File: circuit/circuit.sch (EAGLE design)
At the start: 56 parts, among them IC1 74HC86N, IC2 74HC86N, IC3 74HC30N, IC4 74HC86N

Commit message: updated circuit (layout needs to be done next)
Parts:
- removed CM4, CM5, CM6: 100nF, rcl:C-EU025-025X050
- removed H1, H2, H3, H4: MOUNT-HOLE3.2, holes:MOUNT-HOLE3.2
- removed IC2, IC4: 74HC86N, 74xx-eu:74HC86N
- removed IC3: 74HC30N, 74xx-eu:74HC30N
- removed JP1: IN, pinhead:PINHD-1X8
- removed JT: (no value), pinhead:PINHD-1X4
- removed RP: 300, rcl:R-EU_0207/10
- removed SJ1, SJ2, SJ3, SJ4, SJ5, SJ6, SJ7, SJ8: (no value), jumper:SJ
- added CS4: 100nF, rcl:C-EU025-025X050
- added LD1, LD2: green, robo_ag:LED-3MM
- added LD3, LD4: yellow, robo_ag:LED-3MM
- added RLD1, RLD2, RLD3, RLD4: 2k, rcl:R-EU_0207/10
- added RN1, RN2, RN3, RN4: 120, resistor-sil:E4R
- added RP1, RP2: 300, rcl:R-EU_0207/10
- added X1: PSS 254/8G, con-molex:22-23-2081
- IC1: value 74HC86N -> 74HC04N; device 74xx-eu:74HC86N -> 74xx-eu:74AC04N
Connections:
- removed net BUS_ERROR: IC3A.O
- removed net DISP_COL_SCK: JP1.6
- removed net DISP_COL_SER: JP1.4
- removed net PROG_MOSI: ICM.PB3(MOSI/OC2), RP.2
- removed net PROG_SCK: ICM.PB5(SCK), JP.3_SCK
- removed net RETURN_LED_LAOD: IC2B.I1
- removed net TWI_SCL: ICM.PC5(ADC5/SCL), JT.1, JT.4
- removed net TWI_SDA: ICM.PC4(ADC4/SDA), JT.2, JT.3
- new net !BUS_RGB: IC1A.I, IC1B.I, ICM.PD1(TXD)
- new net !RETURN_RGB: IC1D.O, ICM.PD0(RXD)
- new net N$32: IC1E.O, RLD2.2
- new net N$33: JP.3_SCK, RP1.2
- new net N$34: LD2.C, RLD2.1
- new net N$35: ICM.PC4(ADC4/SDA)
- new net N$36: ICM.PC5(ADC5/SCL)
- new net N$37: IC1C.O, RLD3.2
- new net N$38: LD3.C, RLD3.1
- new net N$41: IC1F.O, RLD4.1
- new net N$42: LD4.A, RLD4.2
- new net PROG_MOSI_AND_DISP_COL_SER: ICM.PB3(MOSI/OC2), RN3B.1, RP2.2
- new net PROG_SCK_AND_DISP_COL_SCK: ICM.PB5(SCK), RN3D.1, RP1.1
- net +5V: now also CS4.1, LD2.A, LD3.A, X1-2.S; no longer CM4.2, CM5.2, CM6.2, IC2P.VCC, IC4P.VCC, JP1.2, SJ8.1
- net BTN2: now also ICM.PB1(OC1A); no longer ICM.PC3(ADC3)
- net BTN3: now also ICM.PB2(SS/OC1B); no longer ICM.PD4(XCK/T0)
- net BUS_BTN_DATA: now also ICM.PD2(INT0), RN1B.1; no longer IC2A.I0, SV1.8
- net BUS_BTN_LOAD: now also ICM.PD3(INT1), RN2C.2; no longer IC1D.I0, SV1.7
- net BUS_CLK: now also ICM.PD6(AIN0), RN2A.1; no longer IC1A.I0, SV1.2
- net BUS_IR_CLK: now also ICM.PD5(T1), RN1C.1; no longer IC1C.I0, SV1.6
- net BUS_LED_DATA: now also IC1C.I, ICM.PD4(XCK/T0), RN1A.1; no longer IC2C.I0, SV1.10
- net BUS_LED_LOAD: now also ICM.PD7(AIN1), RN2B.2; no longer IC2B.I0, SV1.9
- net BUS_RGB: now also IC1A.O, RN1D.1; no longer IC1B.I0, SV1.4
- net DISP_!ENABLE!: now also ICM.PC3(ADC3), RN4B.1; no longer JP1.8
- net DISP_RCK: now also ICM.PC2(ADC2), RN4A.1; no longer JP1.7
- net DISP_ROW_SCK: now also ICM.PC1(ADC1), RN3C.1; no longer JP1.5
- net DISP_ROW_SER: now also ICM.PC0(ADC0), RN3A.1; no longer JP1.3
- net GND: now also CS4.2, LD1.C, LD4.C, SV1.10, SV1.6, SV1.8, SV2.10, SV2.6, SV2.8, X1-1.S; no longer CM4.1, CM5.1, CM6.1, IC2D.I0, IC2D.I1, IC2P.GND, IC4P.GND, JP1.1, SV1.1, SV1.3, SV1.5, SV2.1, SV2.3, SV2.5
- net N$1: now also RN1A.2, SV1.1; no longer IC3A.I0, SJ1.2
- net N$16: now also RN1D.2, SV1.7; no longer IC3A.I3, SJ4.2
- net N$17: now also RN2A.2, SV1.9; no longer IC3A.I4, SJ5.2
- net N$18: now also RN2C.1, SV1.4; no longer IC3A.I5, SJ6.2
- net N$19: now also RN2B.1, SV1.2; no longer IC3A.I6, SJ7.2
- net N$2: now also RN1B.2, SV1.3; no longer IC3A.I1, SJ2.2
- net N$20: now also RN3A.2, X1-3.S; no longer IC3A.I7, SJ8.2
- net N$21: now also RN3B.2, X1-4.S; no longer IC1A.O, SJ1.1
- net N$22: now also RN3C.2, X1-5.S; no longer IC1B.O, SJ2.1
- net N$23: now also RN3D.2, X1-6.S; no longer IC1C.O, SJ3.1
- net N$24: now also RN4A.2, X1-7.S; no longer IC1D.O, SJ4.1
- net N$25: now also RN4B.2, X1-8.S; no longer IC2A.O, SJ5.1
- net N$26: now also LD1.A, RLD1.2; no longer IC2B.O, SJ6.1
- net N$3: now also RN1C.2, SV1.5; no longer IC3A.I2, SJ3.2
- net N$31: now also IC1B.O, RLD1.1; no longer IC2C.O, SJ7.1
- net PROG_MOSI_1: now also RP2.1; no longer RP.1
- net RETURN_BTN_DATA: now also IC1F.I, SV2.3; no longer IC2A.I1, SV2.8
- net RETURN_BTN_LOAD: now also SV2.4; no longer IC1D.I1, SV2.7
- net RETURN_CLK: now also SV2.9; no longer IC1A.I1, SV2.2
- net RETURN_IR_CLK: now also SV2.5; no longer IC1C.I1, SV2.6
- net RETURN_LED_DATA: now also SV2.1; no longer IC2C.I1, SV2.10
- net RETURN_LED_LOAD: now also SV2.2; no longer SV2.9
- net RETURN_RGB: now also IC1D.I, IC1E.I, SV2.7; no longer IC1B.I1, SV2.4
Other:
- note added: "(also OC0A)"
- note added: "1. Inversion of UART: bus-protocoll for RGB-LED (WS2812B) is invers to UART-Protocoll e.g. idle is low instead of high"
- note added: "2. Additional features: power supply button 3 data leds (RGB, IR, Button)"
- note added: "3. only for self-test: BUS_BTN_DATA RETURN_RGB RETURN_LED_DATA"
- note added: "Additionals"
- note added: "In/Out Lights"
- note added: "Logic"
- note added: "OC0B"
- note added: "Out Display"
- note added: "indicator for receiving a pushed button"
- note added: "indicator for receiving data from last RGB-led"
- note added: "indicator for sending data to RGB-leds"
- note added: "indicator for turning IR-leds on"
- note removed: "Anzeige Connector"
- note removed: "BUS-Driver"
- note removed: "Nochmal drüber nachdenken! Über die Jumper können die gewünschten Signale gewählt werden. Allerdings müssen freie Eingänge mit VDD verbunden werden. Hier ist noch eine clevere Lösung nötig."
- note removed: "Reserve"
- moved on the sheet: CM1, CM2, CM3, CQ1, CQ2, IC1P, ICM, JP, Q1, SV1, SV2

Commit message: Updated Layout
Layout work in progress
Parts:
- removed RN1, RN2, RN3, RN4: 120, resistor-sil:E4R
- added R1, R10, R11, R12, R13, R2, R3, R4, R5, R6, R7, R8, R9: 120, rcl:R-EU_R0805
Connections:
- removed net N$35: ICM.PC4(ADC4/SDA)
- removed net N$36: ICM.PC5(ADC5/SCL)
- net BTN1: now also ICM.PC4(ADC4/SDA); no longer ICM.PB0(ICP)
- net BTN2: now also ICM.PC5(ADC5/SCL); no longer ICM.PB1(OC1A)
- net BUS_BTN_DATA: now also R8.1; no longer RN1B.1
- net BUS_BTN_LOAD: now also R13.2; no longer RN2C.2
- net BUS_CLK: now also R11.1; no longer RN2A.1
- net BUS_IR_CLK: now also R9.1; no longer RN1C.1
- net BUS_LED_DATA: now also R7.1; no longer RN1A.1
- net BUS_LED_LOAD: now also R12.2; no longer RN2B.2
- net BUS_RGB: now also R10.1; no longer RN1D.1
- net DISP_!ENABLE!: now also R6.1; no longer RN4B.1
- net DISP_RCK: now also R5.1; no longer RN4A.1
- net DISP_ROW_SCK: now also R3.1; no longer RN3C.1
- net DISP_ROW_SER: now also R1.1; no longer RN3A.1
- net N$1: now also R7.2; no longer RN1A.2
- net N$16: now also R10.2; no longer RN1D.2
- net N$17: now also R11.2; no longer RN2A.2
- net N$18: now also R13.1; no longer RN2C.1
- net N$19: now also R12.1; no longer RN2B.1
- net N$2: now also R8.2; no longer RN1B.2
- net N$20: now also R1.2; no longer RN3A.2
- net N$21: now also R2.2; no longer RN3B.2
- net N$22: now also R3.2; no longer RN3C.2
- net N$23: now also R4.2; no longer RN3D.2
- net N$24: now also R5.2; no longer RN4A.2
- net N$25: now also R6.2; no longer RN4B.2
- net N$3: now also R9.2; no longer RN1C.2
- net PROG_MOSI_AND_DISP_COL_SER: now also R2.1; no longer RN3B.1
- net PROG_SCK_AND_DISP_COL_SCK: now also R4.1; no longer RN3D.1

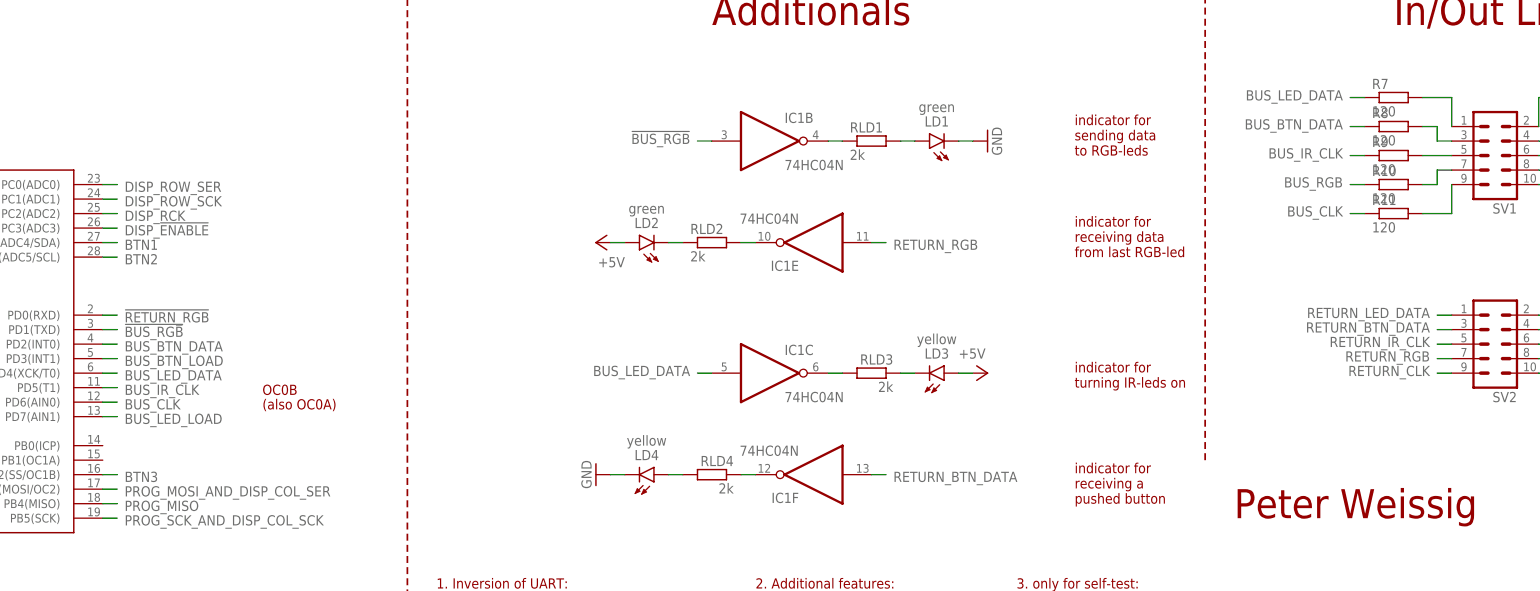
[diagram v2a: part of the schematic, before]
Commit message: Layout nearly completed
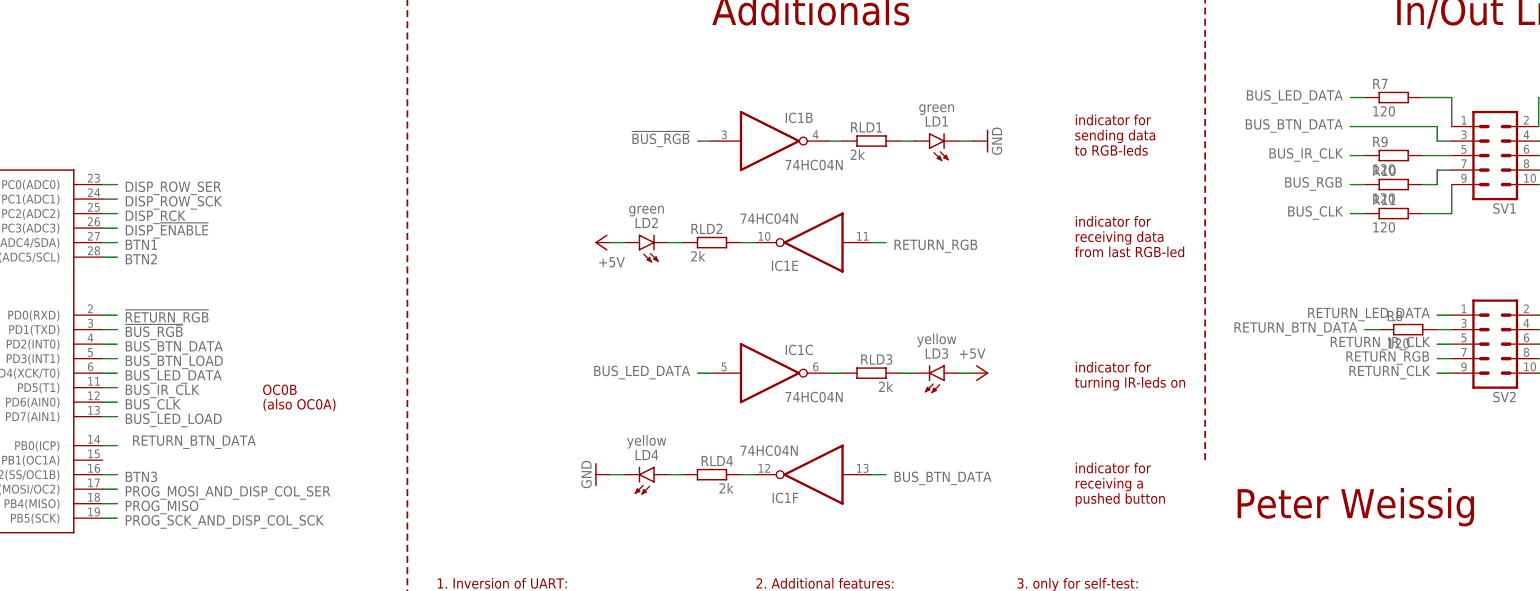
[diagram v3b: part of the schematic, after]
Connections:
- net BUS_BTN_DATA: now also IC1F.I, SV1.3; no longer R8.1
- net N$2: now also SV2.3; no longer SV1.3
- net RETURN_BTN_DATA: now also ICM.PB0(ICP), R8.1; no longer IC1F.I, SV2.3
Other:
- moved on the sheet: R8
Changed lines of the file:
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@@
 <part name="R6" library="rcl" deviceset="R-EU_" device="R0805" value="120"/>
 <part name="R7" library="rcl" deviceset="R-EU_" device="R0805" value="120"/>
-<part name="R8" library="rcl" deviceset="R-EU_" device="R0805" value="120"/>
 <part name="R9" library="rcl" deviceset="R-EU_" device="R0805" value="120"/>
 <part name="R10" library="rcl" deviceset="R-EU_" device="R0805" value="120"/>
@@
 <part name="R12" library="rcl" deviceset="R-EU_" device="R0805" value="120"/>
 <part name="R13" library="rcl" deviceset="R-EU_" device="R0805" value="120"/>
+<part name="R8" library="rcl" deviceset="R-EU_" device="R0805" value="120"/>
 </parts>
 <sheets>
@@
 <instance part="R6" gate="G$1" x="347.98" y="137.16"/>
 <instance part="R7" gate="G$1" x="320.04" y="99.06"/>
-<instance part="R8" gate="G$1" x="320.04" y="93.98"/>
 <instance part="R9" gate="G$1" x="320.04" y="88.9"/>
 <instance part="R10" gate="G$1" x="320.04" y="83.82"/>
@@
 <instance part="R12" gate="G$1" x="355.6" y="99.06"/>
 <instance part="R13" gate="G$1" x="355.6" y="93.98"/>
+<instance part="R8" gate="G$1" x="322.58" y="58.42"/>
 </instances>
 <busses>
@@
 <net name="RETURN_BTN_DATA" class="0">
 <segment>
-<wire x1="330.2" y1="58.42" x2="327.66" y2="58.42" width="0.1524" layer="91"/>
-<label x="326.39" y="59.69" size="1.778" layer="91" rot="R180"/>
-<pinref part="SV2" gate="G$1" pin="3"/>
+<label x="313.69" y="59.69" size="1.778" layer="91" rot="R180"/>
+<wire x1="317.5" y1="58.42" x2="314.96" y2="58.42" width="0.1524" layer="91"/>
+<pinref part="R8" gate="G$1" pin="1"/>
+</segment>
+<segment>
+<pinref part="ICM" gate="G$1" pin="PB0(ICP)"/>
+<wire x1="93.98" y1="38.1" x2="96.52" y2="38.1" width="0.1524" layer="91"/>
+<label x="99.06" y="38.1" size="1.778" layer="95"/>
+</segment>
+</net>
+<net name="RETURN_LED_DATA" class="0">
+<segment>
+<wire x1="330.2" y1="60.96" x2="327.66" y2="60.96" width="0.1524" layer="91"/>
+<label x="326.39" y="62.23" size="1.778" layer="91" rot="R180"/>
+<pinref part="SV2" gate="G$1" pin="1"/>
+</segment>
+</net>
+<net name="RETURN_LED_LOAD" class="0">
+<segment>
+<wire x1="345.44" y1="60.96" x2="347.98" y2="60.96" width="0.1524" layer="91"/>
+<label x="349.25" y="59.69" size="1.778" layer="91"/>
+<pinref part="SV2" gate="G$1" pin="2"/>
+</segment>
+</net>
+<net name="RETURN_BTN_LOAD" class="0">
+<segment>
+<wire x1="345.44" y1="58.42" x2="347.98" y2="58.42" width="0.1524" layer="91"/>
+<label x="349.25" y="57.15" size="1.778" layer="91"/>
+<pinref part="SV2" gate="G$1" pin="4"/>
+</segment>
+</net>
+<net name="RETURN_RGB" class="0">
+<segment>
+<wire x1="330.2" y1="53.34" x2="327.66" y2="53.34" width="0.1524" layer="91"/>
+<label x="326.39" y="54.61" size="1.778" layer="91" rot="R180"/>
+<pinref part="SV2" gate="G$1" pin="7"/>
+</segment>
+<segment>
+<pinref part="IC1" gate="D" pin="I"/>
+<wire x1="210.82" y1="147.32" x2="213.36" y2="147.32" width="0.1524" layer="91"/>
+<label x="214.63" y="146.05" size="1.778" layer="91"/>
+</segment>
+<segment>
+<pinref part="IC1" gate="E" pin="I"/>
+<wire x1="231.14" y1="73.66" x2="228.6" y2="73.66" width="0.1524" layer="91"/>
+<label x="232.41" y="72.39" size="1.778" layer="91"/>
+</segment>
+</net>
+<net name="BUS_BTN_DATA" class="0">
+<segment>
+<label x="311.15" y="95.25" size="1.778" layer="91" rot="R180"/>
+<wire x1="327.66" y1="93.98" x2="327.66" y2="91.44" width="0.1524" layer="91"/>
+<pinref part="SV1" gate="G$1" pin="3"/>
+<wire x1="327.66" y1="91.44" x2="330.2" y2="91.44" width="0.1524" layer="91"/>
+<wire x1="317.5" y1="93.98" x2="325.12" y2="93.98" width="0.1524" layer="91"/>
+<wire x1="325.12" y1="93.98" x2="327.66" y2="93.98" width="0.1524" layer="91"/>
+<wire x1="317.5" y1="93.98" x2="312.42" y2="93.98" width="0.1524" layer="91"/>
+</segment>
+<segment>
+<pinref part="ICM" gate="G$1" pin="PD2(INT0)"/>
+<wire x1="96.52" y1="55.88" x2="93.98" y2="55.88" width="0.1524" layer="91"/>
+<label x="97.79" y="54.61" size="1.778" layer="91"/>
 </segment>
 <segment>
@@
 <wire x1="228.6" y1="33.02" x2="231.14" y2="33.02" width="0.1524" layer="91"/>
 <label x="232.41" y="31.75" size="1.778" layer="91"/>
-</segment>
-</net>
-<net name="RETURN_LED_DATA" class="0">
-<segment>
-<wire x1="330.2" y1="60.96" x2="327.66" y2="60.96" width="0.1524" layer="91"/>
-<label x="326.39" y="62.23" size="1.778" layer="91" rot="R180"/>
-<pinref part="SV2" gate="G$1" pin="1"/>
-</segment>
-</net>
-<net name="RETURN_LED_LOAD" class="0">
-<segment>
-<wire x1="345.44" y1="60.96" x2="347.98" y2="60.96" width="0.1524" layer="91"/>
-<label x="349.25" y="59.69" size="1.778" layer="91"/>
-<pinref part="SV2" gate="G$1" pin="2"/>
-</segment>
-</net>
-<net name="RETURN_BTN_LOAD" class="0">
-<segment>
-<wire x1="345.44" y1="58.42" x2="347.98" y2="58.42" width="0.1524" layer="91"/>
-<label x="349.25" y="57.15" size="1.778" layer="91"/>
-<pinref part="SV2" gate="G$1" pin="4"/>
-</segment>
-</net>
-<net name="RETURN_RGB" class="0">
-<segment>
-<wire x1="330.2" y1="53.34" x2="327.66" y2="53.34" width="0.1524" layer="91"/>
-<label x="326.39" y="54.61" size="1.778" layer="91" rot="R180"/>
-<pinref part="SV2" gate="G$1" pin="7"/>
-</segment>
-<segment>
-<pinref part="IC1" gate="D" pin="I"/>
-<wire x1="210.82" y1="147.32" x2="213.36" y2="147.32" width="0.1524" layer="91"/>
-<label x="214.63" y="146.05" size="1.778" layer="91"/>
-</segment>
-<segment>
-<pinref part="IC1" gate="E" pin="I"/>
-<wire x1="231.14" y1="73.66" x2="228.6" y2="73.66" width="0.1524" layer="91"/>
-<label x="232.41" y="72.39" size="1.778" layer="91"/>
-</segment>
-</net>
-<net name="BUS_BTN_DATA" class="0">
-<segment>
-<label x="311.15" y="95.25" size="1.778" layer="91" rot="R180"/>
-<wire x1="314.96" y1="93.98" x2="312.42" y2="93.98" width="0.1524" layer="91"/>
-<pinref part="R8" gate="G$1" pin="1"/>
-</segment>
-<segment>
-<pinref part="ICM" gate="G$1" pin="PD2(INT0)"/>
-<wire x1="96.52" y1="55.88" x2="93.98" y2="55.88" width="0.1524" layer="91"/>
-<label x="97.79" y="54.61" size="1.778" layer="91"/>
 </segment>
 </net>
@@
 <wire x1="330.2" y1="99.06" x2="330.2" y2="93.98" width="0.1524" layer="91"/>
 <pinref part="R7" gate="G$1" pin="2"/>
-</segment>
-</net>
-<net name="N$2" class="0">
-<segment>
-<wire x1="325.12" y1="93.98" x2="327.66" y2="93.98" width="0.1524" layer="91"/>
-<wire x1="327.66" y1="93.98" x2="327.66" y2="91.44" width="0.1524" layer="91"/>
-<pinref part="SV1" gate="G$1" pin="3"/>
-<wire x1="327.66" y1="91.44" x2="330.2" y2="91.44" width="0.1524" layer="91"/>
-<pinref part="R8" gate="G$1" pin="2"/>
 </segment>
 </net>
@@
 </segment>
 </net>
+<net name="N$2" class="0">
+<segment>
+<pinref part="SV2" gate="G$1" pin="3"/>
+<wire x1="330.2" y1="58.42" x2="327.66" y2="58.42" width="0.1524" layer="91"/>
+<pinref part="R8" gate="G$1" pin="2"/>
+</segment>
+</net>

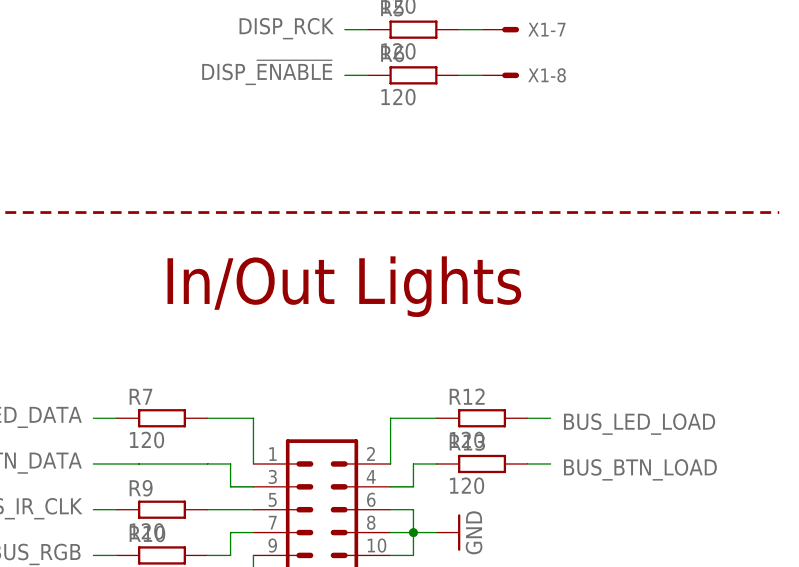
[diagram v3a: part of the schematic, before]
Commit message: updated layout of circuit board   + improved readability of labels   + added info labels to bottom   + added smiley
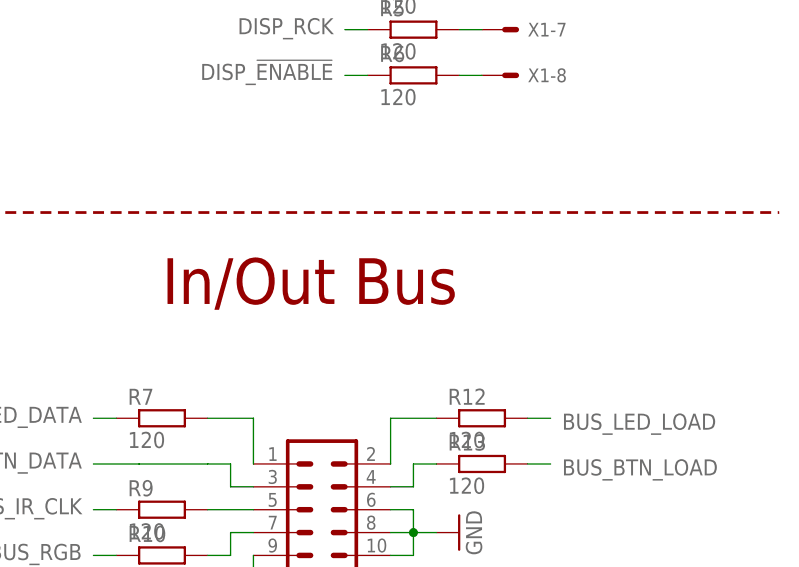
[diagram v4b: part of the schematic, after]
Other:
- note added: "In/Out Bus"
- note removed: "In/Out Lights"
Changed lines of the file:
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@@
 <?xml version="1.0" encoding="utf-8"?>
 <!DOCTYPE eagle SYSTEM "eagle.dtd">
-<eagle version="7.7.0">
+<eagle version="6.6.0">
 <drawing>
 <settings>
@@
 <layer number="95" name="Names" color="7" fill="1" visible="yes" active="yes"/>
 <layer number="96" name="Values" color="7" fill="1" visible="yes" active="yes"/>
-<layer number="97" name="Info" color="7" fill="1" visible="yes" active="yes"/>
-<layer number="98" name="Guide" color="6" fill="1" visible="yes" active="yes"/>
-<layer number="99" name="SpiceOrder" color="5" fill="1" visible="yes" active="yes"/>
+<layer number="97" name="Info" color="7" fill="1" visible="no" active="yes"/>
+<layer number="98" name="Guide" color="6" fill="1" visible="no" active="yes"/>
+<layer number="99" name="SpiceOrder" color="5" fill="1" visible="no" active="yes"/>
 <layer number="100" name="Muster" color="7" fill="1" visible="no" active="no"/>
 <layer number="101" name="Hidden" color="15" fill="1" visible="no" active="yes"/>
@@
 <layer number="103" name="Stiffner" color="6" fill="3" visible="no" active="yes"/>
 <layer number="104" name="Name" color="7" fill="1" visible="no" active="yes"/>
-<layer number="105" name="Beschreib" color="7" fill="1" visible="yes" active="yes"/>
+<layer number="105" name="Beschreib" color="7" fill="1" visible="no" active="yes"/>
 <layer number="106" name="BGA-Top" color="7" fill="1" visible="no" active="yes"/>
 <layer number="107" name="BD-Top" color="7" fill="1" visible="no" active="yes"/>
@@
 <text x="53.34" y="190.5" size="5.08" layer="94">Programmer</text>
 <text x="322.58" y="190.5" size="5.08" layer="94">Out Display</text>
-<text x="320.04" y="111.76" size="5.08" layer="94">In/Out Lights</text>
+<text x="320.04" y="111.76" size="5.08" layer="94">In/Out Bus</text>
 <wire x1="287.02" y1="121.92" x2="388.62" y2="121.92" width="0.3048" layer="94" style="longdash"/>
 <wire x1="147.32" y1="0" x2="147.32" y2="121.92" width="0.3048" layer="94" style="longdash"/>
